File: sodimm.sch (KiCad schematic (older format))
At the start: 3 parts, among them J9 ddr3-sodimm-slot-2-2013289-2

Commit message: Library cleanup, add RGMII layout
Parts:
- J9: footprint antmicro-footprints:TE_2-2013289-2 -> lpddr4-test-board-footprints:TE_2-2013289-2; symbol antmicroMemoryConnectorsPCCardSockets:ddr3-sodimm-slot-2-2013289-2 -> lpddr4-test-board:ddr3-sodimm-slot-2-2013289-2
- R55, R56: footprint antmicro-footprints:0402-res -> lpddr4-test-board-footprints:0402-res; symbol antmicroResistors0402:R_0R_0402 -> lpddr4-test-board:R_0R_0402
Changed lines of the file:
@@
 VDDQ
 $Comp
-L antmicroResistors0402:R_0R_0402 R55
+L lpddr4-test-board:R_0R_0402 R55
 U 1 1 606BFB95
 P 4275 9625
 F 0 "R55" H 4275 9700 60  0000 C CNN
 F 1 "R_0R_0402" H 4275 9475 60  0001 C CNN
-F 2 "antmicro-footprints:0402-res" H 4475 9825 60  0001 L CNN
+F 2 "lpddr4-test-board-footprints:0402-res" H 4475 9825 60  0001 L CNN
 F 3 "" H 4275 9625 50  0001 C CNN
 F 4 "PANASONIC" H 4475 10025 60  0001 L CNN "Manufacturer"
@@
 $EndComp
 $Comp
-L antmicroResistors0402:R_0R_0402 R56
+L lpddr4-test-board:R_0R_0402 R56
 U 1 1 606C1C63
 P 4275 9800
 F 0 "R56" H 4275 9875 60  0000 C CNN
 F 1 "R_0R_0402" H 4275 9650 60  0001 C CNN
-F 2 "antmicro-footprints:0402-res" H 4475 10000 60  0001 L CNN
+F 2 "lpddr4-test-board-footprints:0402-res" H 4475 10000 60  0001 L CNN
 F 3 "" H 4275 9800 50  0001 C CNN
 F 4 "PANASONIC" H 4475 10200 60  0001 L CNN "Manufacturer"
@@
 $EndComp
 $Comp
-L antmicroMemoryConnectorsPCCardSockets:ddr3-sodimm-slot-2-2013289-2 J9
+L lpddr4-test-board:ddr3-sodimm-slot-2-2013289-2 J9
 U 1 1 60D77CED
 P 4350 5100
 F 0 "J9" H 4350 7267 50  0000 C CNN
 F 1 "ddr3-sodimm-slot-2-2013289-2" H 4350 7176 50  0000 C CNN
-F 2 "antmicro-footprints:TE_2-2013289-2" H 4350 5100 50  0001 L BNN
+F 2 "lpddr4-test-board-footprints:TE_2-2013289-2" H 4350 5100 50  0001 L BNN
 F 3 "" H 4350 5100 50  0001 L BNN
 F 4 "Manufacturer Recommendation" H 4350 5100 50  0001 L BNN "STANDARD"
@@
 $EndComp
 $Comp
-L antmicroMemoryConnectorsPCCardSockets:ddr3-sodimm-slot-2-2013289-2 J9
+L lpddr4-test-board:ddr3-sodimm-slot-2-2013289-2 J9
 U 2 1 60D7BA8A
 P 11175 5775
 F 0 "J9" H 11175 9442 50  0000 C CNN
 F 1 "ddr3-sodimm-slot-2-2013289-2" H 11175 9351 50  0000 C CNN
-F 2 "antmicro-footprints:TE_2-2013289-2" H 11175 5775 50  0001 L BNN
+F 2 "lpddr4-test-board-footprints:TE_2-2013289-2" H 11175 5775 50  0001 L BNN
 F 3 "" H 11175 5775 50  0001 L BNN
 F 4 "Manufacturer Recommendation" H 11175 5775 50  0001 L BNN "STANDARD"

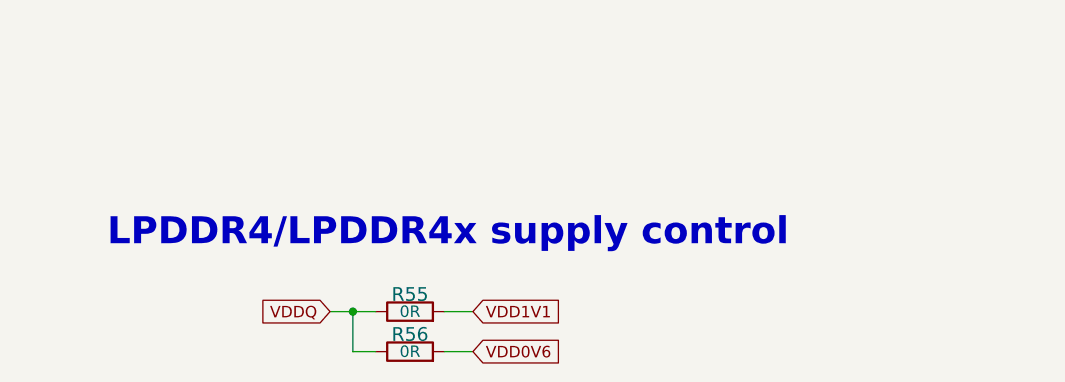
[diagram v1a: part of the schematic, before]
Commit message: Add power supply routing
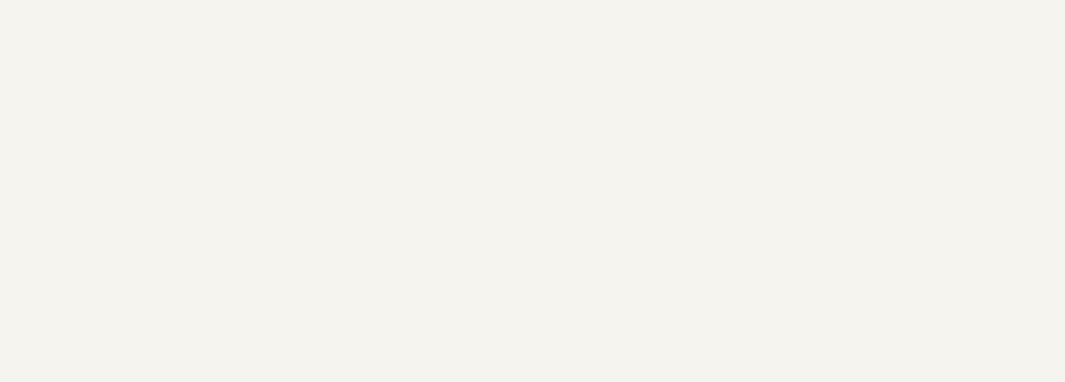
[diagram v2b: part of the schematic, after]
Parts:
- removed R55, R56: R_0R_0402, lpddr4-test-board-footprints:0402-res, symbol lpddr4-test-board:R_0R_0402
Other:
- note removed: "LPDDR4/LPDDR4x supply control"
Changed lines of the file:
@@
 Text GLabel 3000 5175 0    50   Input ~ 0
 VDD1V8
-Text GLabel 4550 9625 2    50   Input ~ 0
-VDD1V1
-Text GLabel 4550 9800 2    50   Input ~ 0
-VDD0V6
 Text Notes 6025 5075 2    50   ~ 0
 VDD1
@@
 Text Notes 2825 2475 0    50   ~ 0
 VDD2\n
-Text GLabel 3925 9625 0    50   Input ~ 0
-VDDQ
-$Comp
-L lpddr4-test-board:R_0R_0402 R55
-U 1 1 606BFB95
-P 4275 9625
-F 0 "R55" H 4275 9700 60  0000 C CNN
-F 1 "R_0R_0402" H 4275 9475 60  0001 C CNN
-F 2 "lpddr4-test-board-footprints:0402-res" H 4475 9825 60  0001 L CNN
-F 3 "" H 4275 9625 50  0001 C CNN
-F 4 "PANASONIC" H 4475 10025 60  0001 L CNN "Manufacturer"
-F 5 "ERJ2GE0R00X" H 4475 9925 60  0001 L CNN "MPN"
-F 6 "0R" H 4275 9625 50  0000 C CNN "Val"
-	1    4275 9625
-	1    0    0    -1
-$EndComp
-$Comp
-L lpddr4-test-board:R_0R_0402 R56
-U 1 1 606C1C63
-P 4275 9800
-F 0 "R56" H 4275 9875 60  0000 C CNN
-F 1 "R_0R_0402" H 4275 9650 60  0001 C CNN
-F 2 "lpddr4-test-board-footprints:0402-res" H 4475 10000 60  0001 L CNN
-F 3 "" H 4275 9800 50  0001 C CNN
-F 4 "PANASONIC" H 4475 10200 60  0001 L CNN "Manufacturer"
-F 5 "ERJ2GE0R00X" H 4475 10100 60  0001 L CNN "MPN"
-F 6 "0R" H 4275 9800 50  0000 C CNN "Val"
-	1    4275 9800
-	1    0    0    -1
-$EndComp
-Wire Wire Line
-	4425 9800 4550 9800
-Wire Wire Line
-	4425 9625 4550 9625
-Wire Wire Line
-	4125 9800 4025 9800
-Wire Wire Line
-	4025 9800 4025 9625
-Wire Wire Line
-	4025 9625 4125 9625
-Wire Wire Line
-	3925 9625 4025 9625
-Connection ~ 4025 9625
-Text Notes 2950 9350 0    118  ~ 24
-LPDDR4/LPDDR4x supply control
 Text GLabel 9775 5475 0    50   Input ~ 0
 DQ4

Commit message: Add DDR4 SODIMM
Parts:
- removed J9: ddr3-sodimm-slot-2-2013289-2, lpddr4-test-board-footprints:TE_2-2013289-2, symbol lpddr4-test-board:ddr3-sodimm-slot-2-2013289-2
- added J?: 2309409-1, antmicro-footprints:TE_2309409-1, symbol antmicroMemoryConnectorsPCCardSockets:2309409-1
- added R55, R56: R_0R_0402, lpddr4-test-board-footprints:0402-res, symbol lpddr4-test-board:R_0R_0402
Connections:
- net labels added: VDD0V6
- wire segments 237 -> 243
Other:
- note added: "LPDDR4/LPDDR4x supply control"

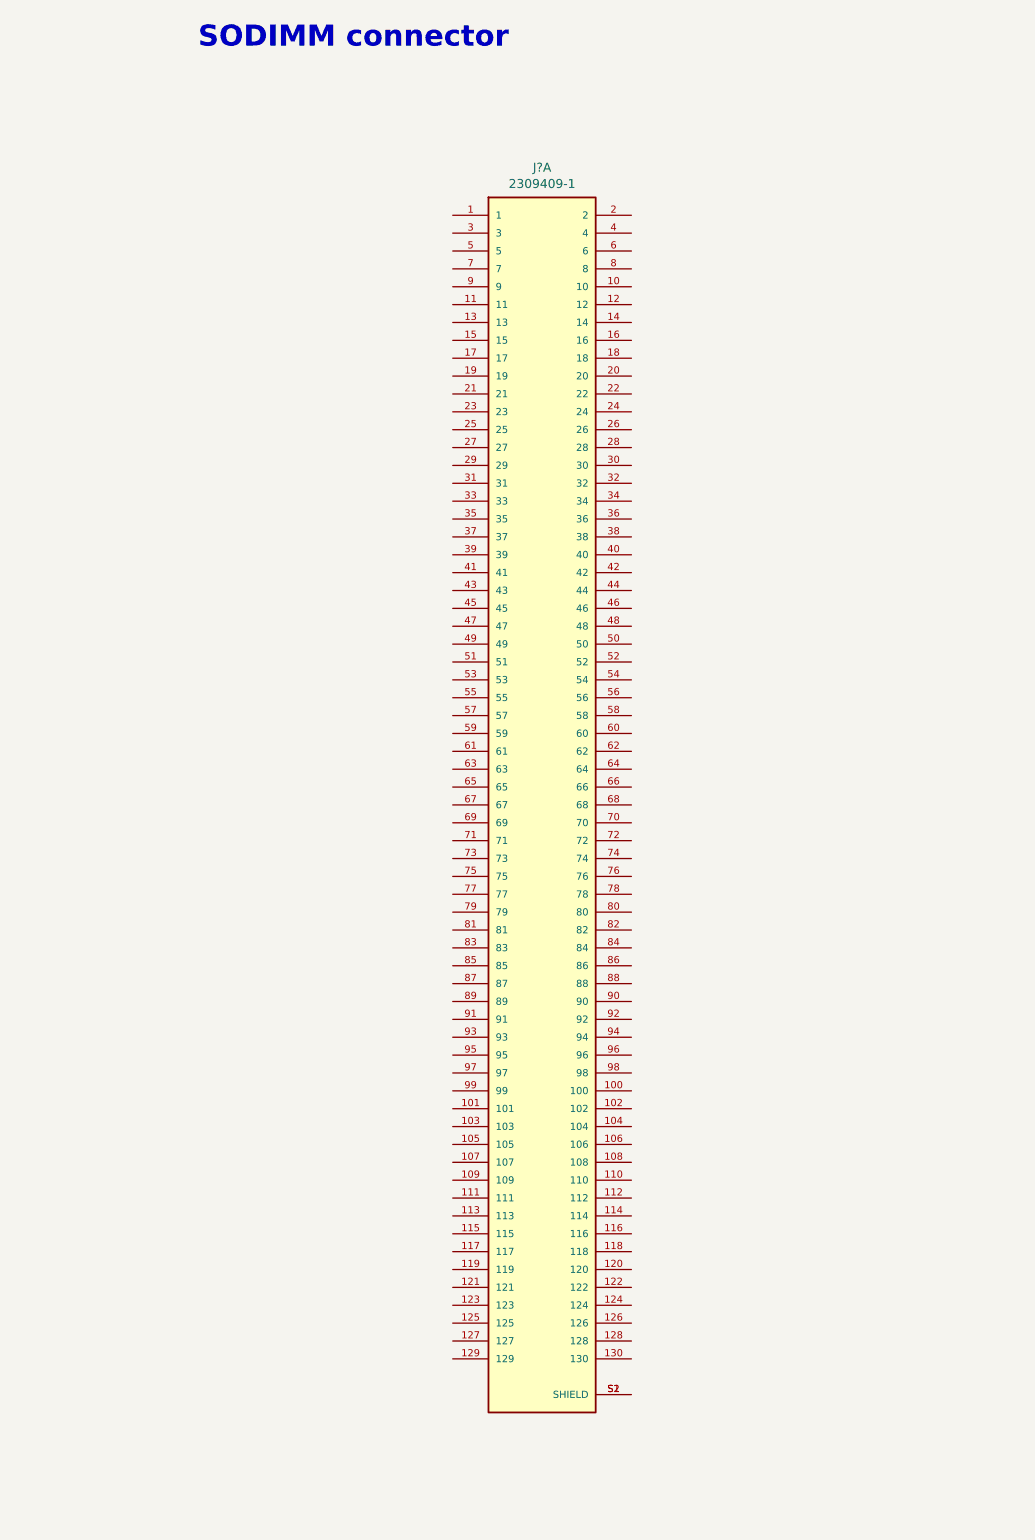
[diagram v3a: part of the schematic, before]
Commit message: re-assinged DDR4 Channel A DQ and CA lanes
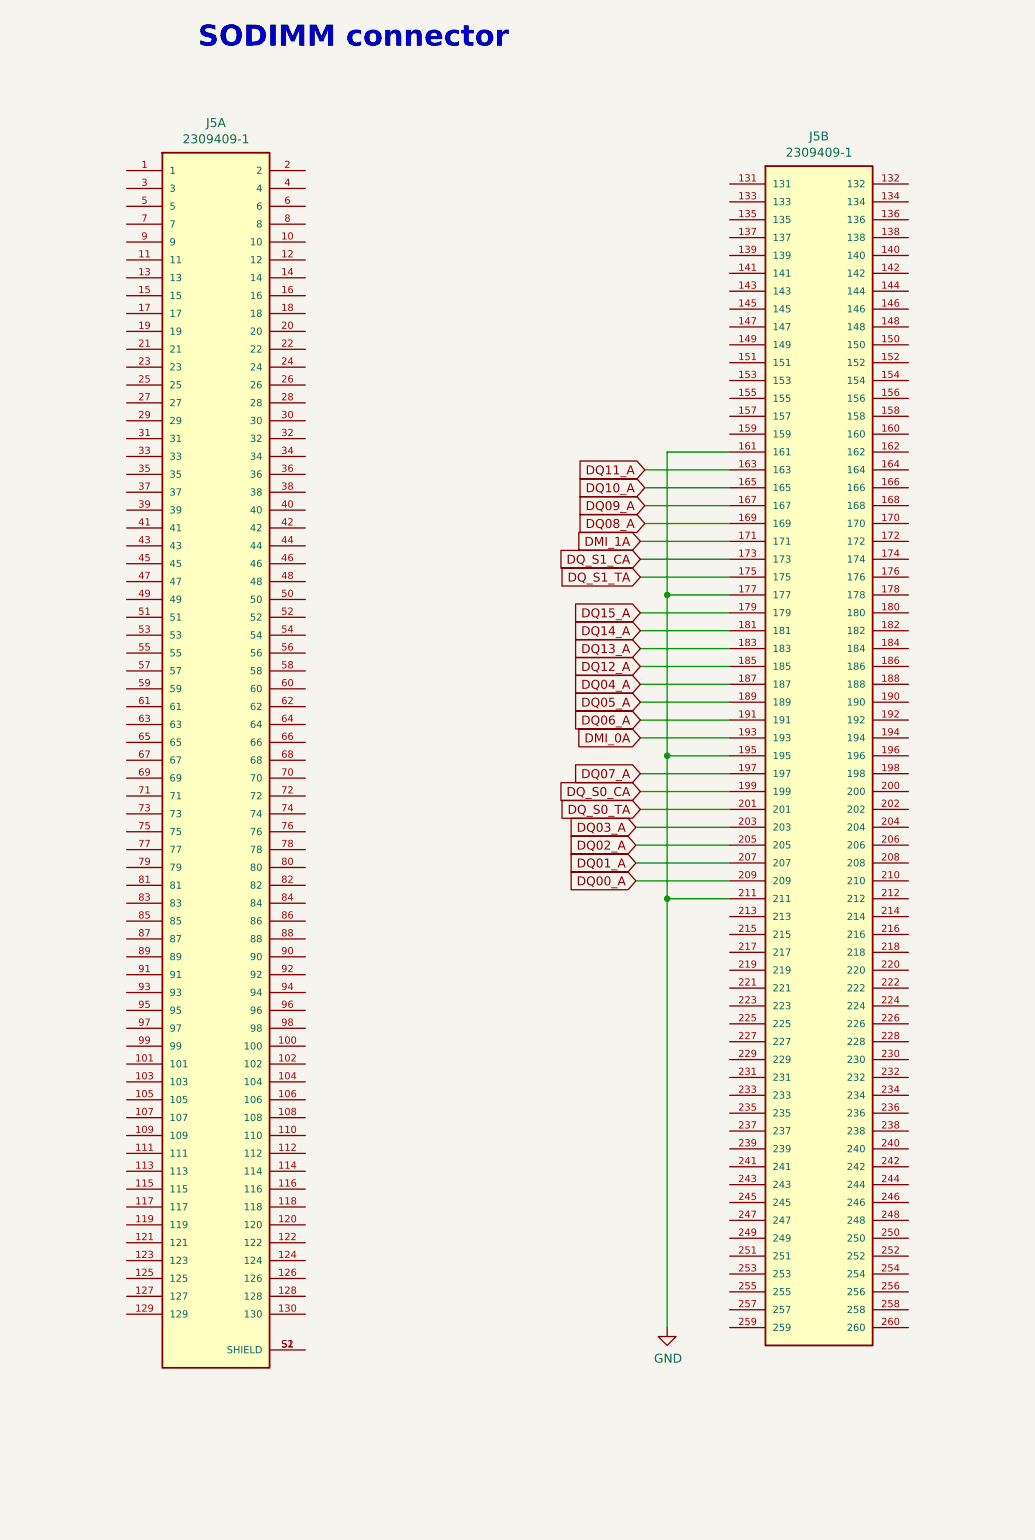
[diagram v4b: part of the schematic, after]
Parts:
- added unit 2 of J5
- gave numbers to parts that had none: 1
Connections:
- net labels added: DMI_0A, DMI_1A, DQ00_A, DQ01_A, DQ02_A, DQ03_A, DQ04_A, DQ05_A, DQ06_A, DQ07_A, DQ08_A, DQ09_A, DQ10_A, DQ11_A, DQ12_A, DQ13_A, DQ14_A, DQ15_A, DQ_S0_CA, DQ_S0_TA, DQ_S1_CA, DQ_S1_TA
- wire segments 243 -> 273
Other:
- moved on the sheet: J5A
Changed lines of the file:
@@
 	3650 4700 3100 4700
 $Comp
-L antmicroMemoryConnectorsPCCardSockets:2309409-1 J?
+L antmicroMemoryConnectorsPCCardSockets:2309409-1 J5
 U 1 1 5FC76C01
-P 9300 5550
-F 0 "J?" H 9300 9117 50  0000 C CNN
-F 1 "2309409-1" H 9300 9026 50  0000 C CNN
-F 2 "antmicro-footprints:TE_2309409-1" H 9000 1950 50  0001 L BNN
-F 3 "" H 10300 5650 50  0001 L BNN
-	1    9300 5550
+P 7475 5300
+F 0 "J5" H 7475 8867 50  0000 C CNN
+F 1 "2309409-1" H 7475 8776 50  0000 C CNN
+F 2 "antmicro-footprints:TE_2309409-1" H 7175 1700 50  0001 L BNN
+F 3 "" H 8475 5400 50  0001 L BNN
+	1    7475 5300
 	1    0    0    -1
 $EndComp
+Text GLabel 9875 3675 0    50   Input ~ 0
+DQ11_A
+$Comp
+L antmicroMemoryConnectorsPCCardSockets:2309409-1 J5
+U 2 1 5FCC3654
+P 10850 5275
+F 0 "J5" H 10850 8742 50  0000 C CNN
+F 1 "2309409-1" H 10850 8651 50  0000 C CNN
+F 2 "antmicro-footprints:TE_2309409-1" H 10550 1675 50  0001 L BNN
+F 3 "" H 11850 5375 50  0001 L BNN
+	2    10850 5275
+	1    0    0    -1
+$EndComp
+Text GLabel 9875 3775 0    50   Input ~ 0
+DQ10_A
+Wire Wire Line
+	10350 3675 9875 3675
+Wire Wire Line
+	10350 3775 9875 3775
+Wire Wire Line
+	10350 3875 9875 3875
+Wire Wire Line
+	10350 3975 9875 3975
+Text GLabel 9875 3875 0    50   Input ~ 0
+DQ09_A
+Text GLabel 9875 3975 0    50   Input ~ 0
+DQ08_A
+Text GLabel 9850 4175 0    50   Input ~ 0
+DQ_S1_CA
+Wire Wire Line
+	9850 4175 10350 4175
+Text GLabel 9850 4275 0    50   Input ~ 0
+DQ_S1_TA
+Wire Wire Line
+	9850 4275 10350 4275
+Text GLabel 9850 4075 0    50   Input ~ 0
+DMI_1A
+$Comp
+L lpddr4-test-board:GND #PWR0103
+U 1 1 5FF1892C
+P 10000 8475
+F 0 "#PWR0103" H 10000 8225 50  0001 C CNN
+F 1 "GND" H 10005 8302 50  0000 C CNN
+F 2 "" H 10000 8475 50  0001 C CNN
+F 3 "" H 10000 8475 50  0001 C CNN
+	1    10000 8475
+	1    0    0    -1
+$EndComp
+Wire Wire Line
+	10350 4375 10000 4375
+Connection ~ 10000 4375
+Wire Wire Line
+	9850 4475 10350 4475
+Wire Wire Line
+	10350 3575 10000 3575
+Wire Wire Line
+	9850 4675 10350 4675
+Text GLabel 9850 4475 0    50   Input ~ 0
+DQ15_A
+Text GLabel 9850 4575 0    50   Input ~ 0
+DQ14_A
+Text GLabel 9850 4675 0    50   Input ~ 0
+DQ13_A
+Text GLabel 9850 4775 0    50   Input ~ 0
+DQ12_A
+Wire Wire Line
+	9850 4775 10350 4775
+Wire Wire Line
+	9850 4875 10350 4875
+Wire Wire Line
+	9850 4975 10350 4975
+Wire Wire Line
+	9850 4575 10350 4575
+Text GLabel 9850 4875 0    50   Input ~ 0
+DQ04_A
+Wire Wire Line
+	10000 4375 10000 5275
+Text GLabel 9850 4975 0    50   Input ~ 0
+DQ05_A
+Text GLabel 9850 5075 0    50   Input ~ 0
+DQ06_A
+Text GLabel 9850 5375 0    50   Input ~ 0
+DQ07_A
+Text GLabel 9850 5475 0    50   Input ~ 0
+DQ_S0_CA
+Wire Wire Line
+	9850 5075 10350 5075
+Wire Wire Line
+	9850 5175 10350 5175
+Wire Wire Line
+	10000 5275 10350 5275
+Wire Wire Line
+	9850 5375 10350 5375
+Connection ~ 10000 5275
+Wire Wire Line
+	10000 3575 10000 4375
+Wire Wire Line
+	9850 4075 10350 4075
+Text GLabel 9850 5175 0    50   Input ~ 0
+DMI_0A
+Text GLabel 9850 5575 0    50   Input ~ 0
+DQ_S0_TA
+Wire Wire Line
+	9850 5475 10350 5475
+Wire Wire Line
+	9850 5575 10350 5575
+Text GLabel 9825 5675 0    50   Input ~ 0
+DQ03_A
+Text GLabel 9825 5775 0    50   Input ~ 0
+DQ02_A
+Text GLabel 9825 5875 0    50   Input ~ 0
+DQ01_A
+Text GLabel 9825 5975 0    50   Input ~ 0
+DQ00_A
+Wire Wire Line
+	9825 5675 10350 5675
+Wire Wire Line
+	9825 5775 10350 5775
+Wire Wire Line
+	9825 5875 10350 5875
+Wire Wire Line
+	9825 5975 10350 5975
+Wire Wire Line
+	10350 6075 10000 6075
+Wire Wire Line
+	10000 5275 10000 6075
+Connection ~ 10000 6075
+Wire Wire Line
+	10000 6075 10000 8475
 $EndSCHEMATC

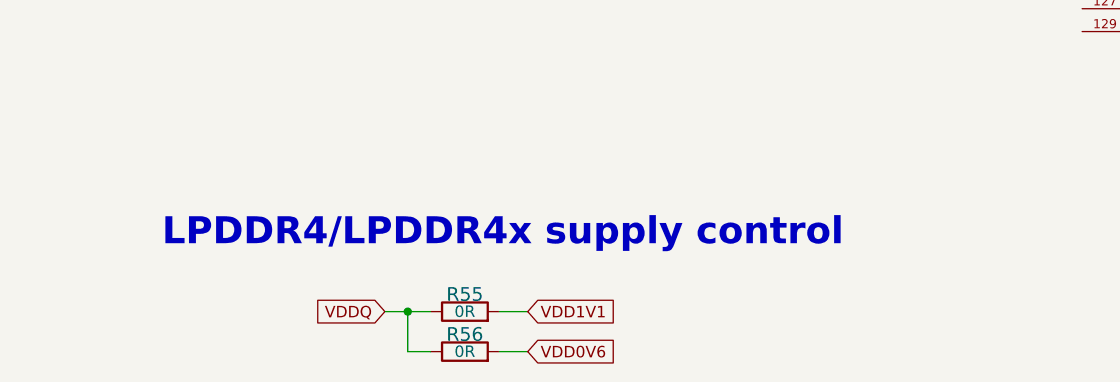
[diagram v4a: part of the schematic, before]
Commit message: Add voltage level selector
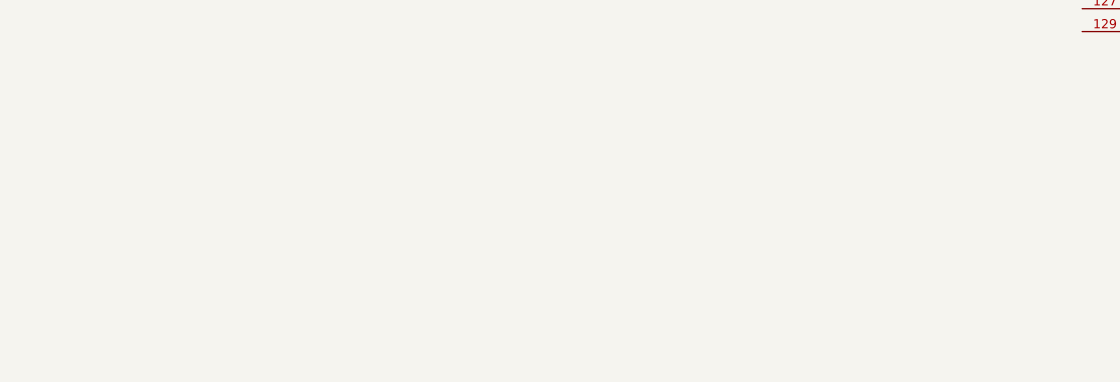
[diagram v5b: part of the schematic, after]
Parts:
- removed R55, R56: R_0R_0402, lpddr4-test-board-footprints:0402-res, symbol lpddr4-test-board:R_0R_0402
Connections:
- net labels removed: VDD0V6
- wire segments 273 -> 267
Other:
- note removed: "LPDDR4/LPDDR4x supply control"
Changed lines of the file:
@@
 Text GLabel 3000 5175 0    50   Input ~ 0
 VDD1V8
-Text GLabel 4550 9625 2    50   Input ~ 0
-VDD1V1
-Text GLabel 4550 9800 2    50   Input ~ 0
-VDD0V6
 Text Notes 6025 5075 2    50   ~ 0
 VDD1
@@
 Text Notes 2825 2475 0    50   ~ 0
 VDD2\n
-Text GLabel 3925 9625 0    50   Input ~ 0
-VDDQ
-$Comp
-L lpddr4-test-board:R_0R_0402 R55
-U 1 1 606BFB95
-P 4275 9625
-F 0 "R55" H 4275 9700 60  0000 C CNN
-F 1 "R_0R_0402" H 4275 9475 60  0001 C CNN
-F 2 "lpddr4-test-board-footprints:0402-res" H 4475 9825 60  0001 L CNN
-F 3 "" H 4275 9625 50  0001 C CNN
-F 4 "PANASONIC" H 4475 10025 60  0001 L CNN "Manufacturer"
-F 5 "ERJ2GE0R00X" H 4475 9925 60  0001 L CNN "MPN"
-F 6 "0R" H 4275 9625 50  0000 C CNN "Val"
-	1    4275 9625
-	1    0    0    -1
-$EndComp
-$Comp
-L lpddr4-test-board:R_0R_0402 R56
-U 1 1 606C1C63
-P 4275 9800
-F 0 "R56" H 4275 9875 60  0000 C CNN
-F 1 "R_0R_0402" H 4275 9650 60  0001 C CNN
-F 2 "lpddr4-test-board-footprints:0402-res" H 4475 10000 60  0001 L CNN
-F 3 "" H 4275 9800 50  0001 C CNN
-F 4 "PANASONIC" H 4475 10200 60  0001 L CNN "Manufacturer"
-F 5 "ERJ2GE0R00X" H 4475 10100 60  0001 L CNN "MPN"
-F 6 "0R" H 4275 9800 50  0000 C CNN "Val"
-	1    4275 9800
-	1    0    0    -1
-$EndComp
-Wire Wire Line
-	4425 9800 4550 9800
-Wire Wire Line
-	4425 9625 4550 9625
-Wire Wire Line
-	4125 9800 4025 9800
-Wire Wire Line
-	4025 9800 4025 9625
-Wire Wire Line
-	4025 9625 4125 9625
-Wire Wire Line
-	3925 9625 4025 9625
-Connection ~ 4025 9625
-Text Notes 2950 9350 0    118  ~ 24
-LPDDR4/LPDDR4x supply control
 Text GLabel 1400 4825 0    50   Input ~ 0
 DQ4
